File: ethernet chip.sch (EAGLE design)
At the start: 28 parts

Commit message: Updated Ethernet Chip Schematic
10/31/15
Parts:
- added U$1: LAN8720LAN8720, Luke:LAN8720LAN8720
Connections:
- new net N$1: R1.2, U$1.RXD0/MODE0
- new net N$10: R7.2, U$1.TXD1
- new net N$11: R11.1, U$1.VDD1A, U$1.VDD2A
- new net N$13: C2.1, R9.1, U$1.XTAL1/CLKIN
- new net N$14: R18.2, U$1.LED2/NINTSEL
- new net N$2: R2.2, U$1.RXD1/MODE1
- new net N$5: R3.2, U$1.CRS_DV/MODE2
- new net N$7: R4.2, U$1.NINT/REFCLKO
- new net N$8: R5.2, U$1.TXEN
- new net N$9: R6.2, U$1.TXD0
- net +3V3: now also U$1.VDDIO
- net GND: now also U$1.VSS_PAD
- net N$3: now also U$1.VDDCR
- net N$4: now also R10.1, U$1.RBIAS; no longer C2.1, R9.1
- net N$6: now also U$1.XTAL2
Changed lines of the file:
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@@
 <part name="+3V3" library="supply1" deviceset="+3V3" device=""/>
 <part name="+3V4" library="supply1" deviceset="+3V3" device=""/>
+<part name="U$1" library="Luke" deviceset="LAN8720" device="LAN8720"/>
 </parts>
 <sheets>
@@
 <instance part="+3V3" gate="G$1" x="-38.1" y="60.96"/>
 <instance part="+3V4" gate="G$1" x="45.72" y="-25.4"/>
+<instance part="U$1" gate="G$1" x="-17.78" y="-2.54"/>
 </instances>
 <busses>
@@
 <wire x1="-83.82" y1="55.88" x2="-66.04" y2="55.88" width="0.1524" layer="91"/>
 <wire x1="-66.04" y1="55.88" x2="-45.72" y2="55.88" width="0.1524" layer="91"/>
-<wire x1="-45.72" y1="55.88" x2="-45.72" y2="25.4" width="0.1524" layer="91"/>
+<wire x1="-45.72" y1="55.88" x2="-45.72" y2="20.32" width="0.1524" layer="91"/>
 <pinref part="C3" gate="G$1" pin="2"/>
 <wire x1="-66.04" y1="50.8" x2="-66.04" y2="55.88" width="0.1524" layer="91"/>
 <junction x="-66.04" y="55.88"/>
-</segment>
-</net>
-<net name="N$4" class="0">
-<segment>
-<pinref part="C2" gate="G$1" pin="1"/>
-<wire x1="-96.52" y1="-81.28" x2="-96.52" y2="-86.36" width="0.1524" layer="91"/>
-<wire x1="-96.52" y1="-86.36" x2="-68.58" y2="-86.36" width="0.1524" layer="91"/>
-<wire x1="-68.58" y1="-86.36" x2="-33.02" y2="-86.36" width="0.1524" layer="91"/>
-<wire x1="-33.02" y1="-86.36" x2="-10.16" y2="-86.36" width="0.1524" layer="91"/>
-<wire x1="-10.16" y1="-86.36" x2="-10.16" y2="-48.26" width="0.1524" layer="91"/>
-<pinref part="R9" gate="G$1" pin="1"/>
-<wire x1="-33.02" y1="-71.12" x2="-33.02" y2="-86.36" width="0.1524" layer="91"/>
-<junction x="-33.02" y="-86.36"/>
-<wire x1="-68.58" y1="-71.12" x2="-68.58" y2="-86.36" width="0.1524" layer="91"/>
-<junction x="-68.58" y="-86.36"/>
+<pinref part="U$1" gate="G$1" pin="VDDCR"/>
+<wire x1="-45.72" y1="20.32" x2="-38.1" y2="20.32" width="0.1524" layer="91"/>
 </segment>
 </net>
@@
 <wire x1="-96.52" y1="-55.88" x2="-96.52" y2="-45.72" width="0.1524" layer="91"/>
 <wire x1="-96.52" y1="-45.72" x2="-68.58" y2="-45.72" width="0.1524" layer="91"/>
-<pinref part="R9" gate="G$1" pin="2"/>
-<wire x1="-68.58" y1="-45.72" x2="-33.02" y2="-45.72" width="0.1524" layer="91"/>
-<wire x1="-33.02" y1="-45.72" x2="-10.16" y2="-45.72" width="0.1524" layer="91"/>
-<wire x1="-33.02" y1="-60.96" x2="-33.02" y2="-45.72" width="0.1524" layer="91"/>
-<junction x="-33.02" y="-45.72"/>
+<wire x1="-68.58" y1="-45.72" x2="-53.34" y2="-45.72" width="0.1524" layer="91"/>
 <wire x1="-68.58" y1="-60.96" x2="-68.58" y2="-45.72" width="0.1524" layer="91"/>
 <junction x="-68.58" y="-45.72"/>
+<pinref part="U$1" gate="G$1" pin="XTAL2"/>
+<wire x1="-38.1" y1="-20.32" x2="-53.34" y2="-20.32" width="0.1524" layer="91"/>
+<wire x1="-53.34" y1="-20.32" x2="-53.34" y2="-45.72" width="0.1524" layer="91"/>
+<wire x1="-53.34" y1="-45.72" x2="-53.34" y2="-60.96" width="0.1524" layer="91"/>
+<junction x="-53.34" y="-45.72"/>
+<pinref part="R9" gate="G$1" pin="2"/>
+<wire x1="-53.34" y1="-60.96" x2="-33.02" y2="-60.96" width="0.1524" layer="91"/>
 </segment>
 </net>
@@
 <wire x1="35.56" y1="-50.8" x2="35.56" y2="-55.88" width="0.1524" layer="91"/>
 <pinref part="GND12" gate="1" pin="GND"/>
+</segment>
+<segment>
+<pinref part="U$1" gate="G$1" pin="VSS_PAD"/>
+<wire x1="-38.1" y1="-35.56" x2="-40.64" y2="-35.56" width="0.1524" layer="91"/>
+<wire x1="-40.64" y1="-35.56" x2="-40.64" y2="-40.64" width="0.1524" layer="91"/>
+<pinref part="GND10" gate="1" pin="GND"/>
+<wire x1="-40.64" y1="-40.64" x2="10.16" y2="-40.64" width="0.1524" layer="91"/>
+<wire x1="10.16" y1="-40.64" x2="10.16" y2="-83.82" width="0.1524" layer="91"/>
 </segment>
 </net>
@@
 </segment>
 <segment>
-<wire x1="-43.18" y1="66.04" x2="-43.18" y2="33.02" width="0.1524" layer="91"/>
+<wire x1="-43.18" y1="66.04" x2="-43.18" y2="22.86" width="0.1524" layer="91"/>
 <pinref part="+3V2" gate="G$1" pin="+3V3"/>
+<pinref part="U$1" gate="G$1" pin="VDDIO"/>
+<wire x1="-43.18" y1="22.86" x2="-38.1" y2="22.86" width="0.1524" layer="91"/>
 </segment>
 <segment>
@@
 </segment>
 </net>
+<net name="N$1" class="0">
+<segment>
+<pinref part="R1" gate="G$1" pin="2"/>
+<wire x1="-71.12" y1="22.86" x2="-55.88" y2="22.86" width="0.1524" layer="91"/>
+<wire x1="-55.88" y1="22.86" x2="-55.88" y2="12.7" width="0.1524" layer="91"/>
+<pinref part="U$1" gate="G$1" pin="RXD0/MODE0"/>
+<wire x1="-55.88" y1="12.7" x2="-38.1" y2="12.7" width="0.1524" layer="91"/>
+</segment>
+</net>
+<net name="N$2" class="0">
+<segment>
+<pinref part="R2" gate="G$1" pin="2"/>
+<wire x1="-71.12" y1="12.7" x2="-58.42" y2="12.7" width="0.1524" layer="91"/>
+<wire x1="-58.42" y1="12.7" x2="-58.42" y2="10.16" width="0.1524" layer="91"/>
+<pinref part="U$1" gate="G$1" pin="RXD1/MODE1"/>
+<wire x1="-58.42" y1="10.16" x2="-38.1" y2="10.16" width="0.1524" layer="91"/>
+</segment>
+</net>
+<net name="N$5" class="0">
+<segment>
+<pinref part="R3" gate="G$1" pin="2"/>
+<wire x1="-71.12" y1="5.08" x2="-71.12" y2="7.62" width="0.1524" layer="91"/>
+<pinref part="U$1" gate="G$1" pin="CRS_DV/MODE2"/>
+<wire x1="-71.12" y1="7.62" x2="-38.1" y2="7.62" width="0.1524" layer="91"/>
+</segment>
+</net>
+<net name="N$7" class="0">
+<segment>
+<pinref part="R4" gate="G$1" pin="2"/>
+<wire x1="-71.12" y1="-2.54" x2="-60.96" y2="-2.54" width="0.1524" layer="91"/>
+<wire x1="-60.96" y1="-2.54" x2="-60.96" y2="-5.08" width="0.1524" layer="91"/>
+<pinref part="U$1" gate="G$1" pin="NINT/REFCLKO"/>
+<wire x1="-60.96" y1="-5.08" x2="-38.1" y2="-5.08" width="0.1524" layer="91"/>
+</segment>
+</net>
+<net name="N$8" class="0">
+<segment>
+<pinref part="R5" gate="G$1" pin="2"/>
+<wire x1="-71.12" y1="-12.7" x2="-60.96" y2="-12.7" width="0.1524" layer="91"/>
+<wire x1="-60.96" y1="-12.7" x2="-60.96" y2="-10.16" width="0.1524" layer="91"/>
+<pinref part="U$1" gate="G$1" pin="TXEN"/>
+<wire x1="-60.96" y1="-10.16" x2="-38.1" y2="-10.16" width="0.1524" layer="91"/>
+</segment>
+</net>
+<net name="N$9" class="0">
+<segment>
+<pinref part="R6" gate="G$1" pin="2"/>
+<wire x1="-71.12" y1="-20.32" x2="-58.42" y2="-20.32" width="0.1524" layer="91"/>
+<wire x1="-58.42" y1="-20.32" x2="-58.42" y2="-12.7" width="0.1524" layer="91"/>
+<pinref part="U$1" gate="G$1" pin="TXD0"/>
+<wire x1="-58.42" y1="-12.7" x2="-38.1" y2="-12.7" width="0.1524" layer="91"/>
+</segment>
+</net>
+<net name="N$10" class="0">
+<segment>
+<pinref part="R7" gate="G$1" pin="2"/>
+<wire x1="-71.12" y1="-27.94" x2="-55.88" y2="-27.94" width="0.1524" layer="91"/>
+<wire x1="-55.88" y1="-27.94" x2="-55.88" y2="-15.24" width="0.1524" layer="91"/>
+<pinref part="U$1" gate="G$1" pin="TXD1"/>
+<wire x1="-55.88" y1="-15.24" x2="-38.1" y2="-15.24" width="0.1524" layer="91"/>
+</segment>
+</net>
+<net name="N$11" class="0">
+<segment>
+<pinref part="U$1" gate="G$1" pin="VDD1A"/>
+<pinref part="R11" gate="G$1" pin="1"/>
+<wire x1="-38.1" y1="27.94" x2="-38.1" y2="38.1" width="0.1524" layer="91"/>
+<pinref part="U$1" gate="G$1" pin="VDD2A"/>
+<wire x1="-38.1" y1="25.4" x2="-38.1" y2="27.94" width="0.1524" layer="91"/>
+<junction x="-38.1" y="27.94"/>
+</segment>
+</net>
+<net name="N$13" class="0">
+<segment>
+<pinref part="U$1" gate="G$1" pin="XTAL1/CLKIN"/>
+<wire x1="-50.8" y1="-58.42" x2="-50.8" y2="-22.86" width="0.1524" layer="91"/>
+<wire x1="-50.8" y1="-22.86" x2="-38.1" y2="-22.86" width="0.1524" layer="91"/>
+<wire x1="-50.8" y1="-58.42" x2="-30.48" y2="-58.42" width="0.1524" layer="91"/>
+<pinref part="C2" gate="G$1" pin="1"/>
+<wire x1="-96.52" y1="-81.28" x2="-96.52" y2="-86.36" width="0.1524" layer="91"/>
+<wire x1="-96.52" y1="-86.36" x2="-68.58" y2="-86.36" width="0.1524" layer="91"/>
+<wire x1="-68.58" y1="-86.36" x2="-33.02" y2="-86.36" width="0.1524" layer="91"/>
+<pinref part="R9" gate="G$1" pin="1"/>
+<wire x1="-33.02" y1="-71.12" x2="-33.02" y2="-76.2" width="0.1524" layer="91"/>
+<wire x1="-33.02" y1="-76.2" x2="-33.02" y2="-86.36" width="0.1524" layer="91"/>
+<wire x1="-68.58" y1="-71.12" x2="-68.58" y2="-86.36" width="0.1524" layer="91"/>
+<junction x="-68.58" y="-86.36"/>
+<wire x1="-33.02" y1="-76.2" x2="-30.48" y2="-76.2" width="0.1524" layer="91"/>
+<junction x="-33.02" y="-76.2"/>
+<wire x1="-30.48" y1="-58.42" x2="-30.48" y2="-76.2" width="0.1524" layer="91"/>
+</segment>
+</net>
+<net name="N$4" class="0">
+<segment>
+<pinref part="U$1" gate="G$1" pin="RBIAS"/>
+<wire x1="-38.1" y1="-30.48" x2="-43.18" y2="-30.48" width="0.1524" layer="91"/>
+<wire x1="-43.18" y1="-30.48" x2="-43.18" y2="-43.18" width="0.1524" layer="91"/>
+<pinref part="R10" gate="G$1" pin="1"/>
+<wire x1="-43.18" y1="-43.18" x2="2.54" y2="-43.18" width="0.1524" layer="91"/>
+<wire x1="2.54" y1="-43.18" x2="2.54" y2="-60.96" width="0.1524" layer="91"/>
+</segment>
+</net>
+<net name="N$14" class="0">
+<segment>
+<pinref part="R18" gate="G$1" pin="2"/>
+<wire x1="35.56" y1="-40.64" x2="35.56" y2="-22.86" width="0.1524" layer="91"/>
+<pinref part="U$1" gate="G$1" pin="LED2/NINTSEL"/>
+<wire x1="35.56" y1="-22.86" x2="2.54" y2="-22.86" width="0.1524" layer="91"/>
+</segment>
+</net>

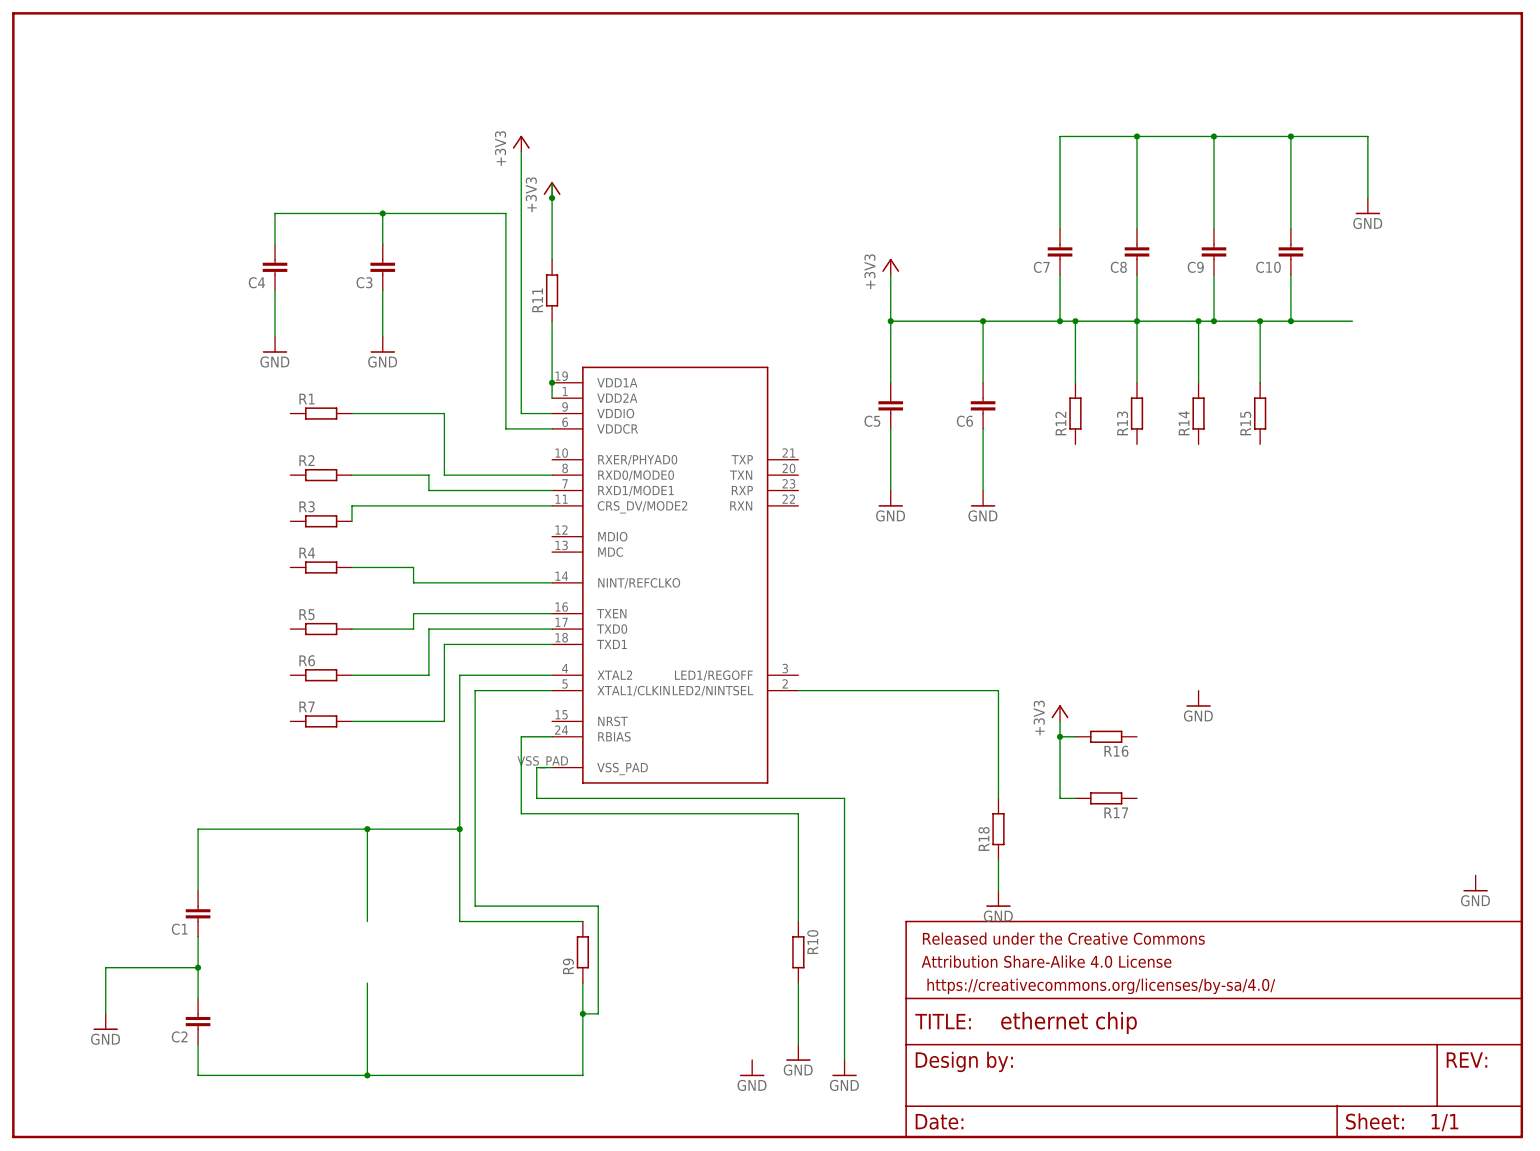
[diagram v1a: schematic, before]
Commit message: Updated Ethernet Chip 11/14/15
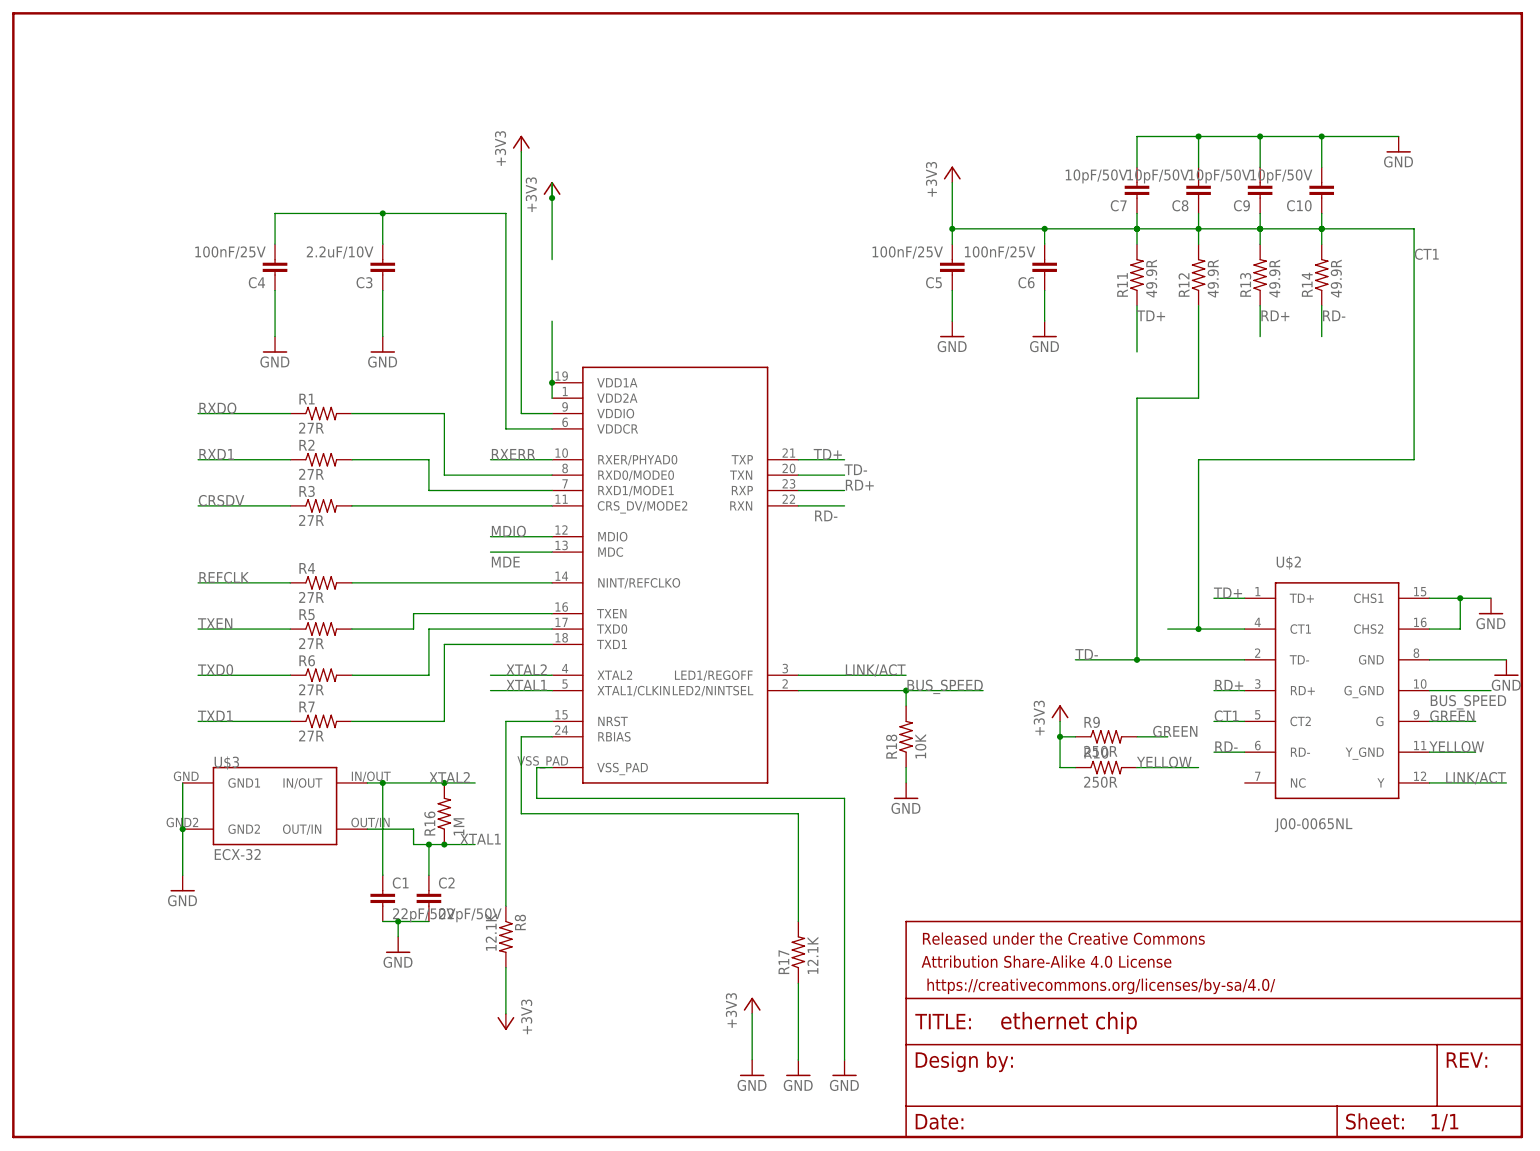
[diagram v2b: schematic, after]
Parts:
- removed R15: (no value), eagle-ltspice:RR0603
- added R8: 12.1K, SparkFun-Passives:RESISTOR0603-RES
- added U$2: J00-0065NL, Paul's Library:J00-0065NL
- added U$3: ECX-32, Other:ECX-32
- C1, C2: value (none) -> 22pF/50V
- C10, C7, C8, C9: value (none) -> 10pF/50V
- C3: value (none) -> 2.2uF/10V
- C4, C5, C6: value (none) -> 100nF/25V
- R1, R2, R3, R4, R5, R6, R7: value (none) -> 27R; device eagle-ltspice:RR0603 -> resistor:R-US_R0603
- R10, R9: value (none) -> 250R; device eagle-ltspice:RR0603 -> resistor:R-US_R0603
- R11, R12, R13, R14: value (none) -> 49.9R; device eagle-ltspice:RR0603 -> resistor:R-US_R0603
- R16: value (none) -> 1M; device eagle-ltspice:RR0603 -> resistor:R-US_R0603
- R17: value (none) -> 12.1K; device eagle-ltspice:RR0603 -> resistor:R-US_R0603
- R18: value (none) -> 10K; device eagle-ltspice:RR0603 -> resistor:R-US_R0603
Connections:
- removed net N$13: C2.1, R9.1, U$1.XTAL1/CLKIN
- removed net N$6: C1.2, R9.2, U$1.XTAL2
- new net BUS_SPEED: R18.2, U$1.LED2/NINTSEL, U$2.G_GND
- new net CRSDV: R3.1
- new net CT1: C10.1, C5.2, C6.2, C7.1, C8.1, C9.1, R11.2, R12.2, R13.2, R14.2, U$2.CT1, U$2.CT2
- new net GREEN: R9.2, U$2.G
- new net LINK/ACT: U$1.LED1/REGOFF, U$2.Y
- new net MDE: U$1.MDC
- new net MDIO: U$1.MDIO
- new net RD+: R13.1, U$1.RXP, U$2.RD+
- new net RD-: R14.1, U$1.RXN, U$2.RD-
- new net REFCLK: R4.1
- new net RXD1: R2.1
- new net RXDO: R1.1
- new net RXERR: U$1.RXER/PHYAD0
- new net TD+: R11.1, U$1.TXP, U$2.TD+
- new net TD-: R12.1, U$1.TXN, U$2.TD-
- new net TXD0: R6.1
- new net TXD1: R7.1
- new net TXEN: R5.1
- new net XTAL1: C2.1, R16.1, U$1.XTAL1/CLKIN, U$3.OUT/IN
- new net XTAL2: C1.1, R16.2, U$1.XTAL2, U$3.IN/OUT
- new net YELLOW: R10.2, U$2.Y_GND
- net +3V3: now also R10.1, R8.2, R9.1; no longer C10.1, C5.2, C6.2, C7.1, C8.1, C9.1, R11.2, R12.2, R13.2, R14.2, R15.2, R16.2, R17.2
- net GND: now also C1.2, R17.1, U$2.CHS1, U$2.CHS2, U$2.GND, U$3.GND1, U$3.GND2; no longer C1.1, R10.2
- net N$11: no longer R11.1
- net N$14: now also R8.1, U$1.NRST; no longer R18.2, U$1.LED2/NINTSEL
- net N$4: now also R17.2; no longer R10.1
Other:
- moved on the sheet: C1, C10, C2, C5, C6, C7, C8, C9
